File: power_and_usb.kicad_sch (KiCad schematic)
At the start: 9 parts, among them J1 USB4085-GF-A_REVB, U1 USBLC6-2SC6, U2 MCP1755T-3302E/DC

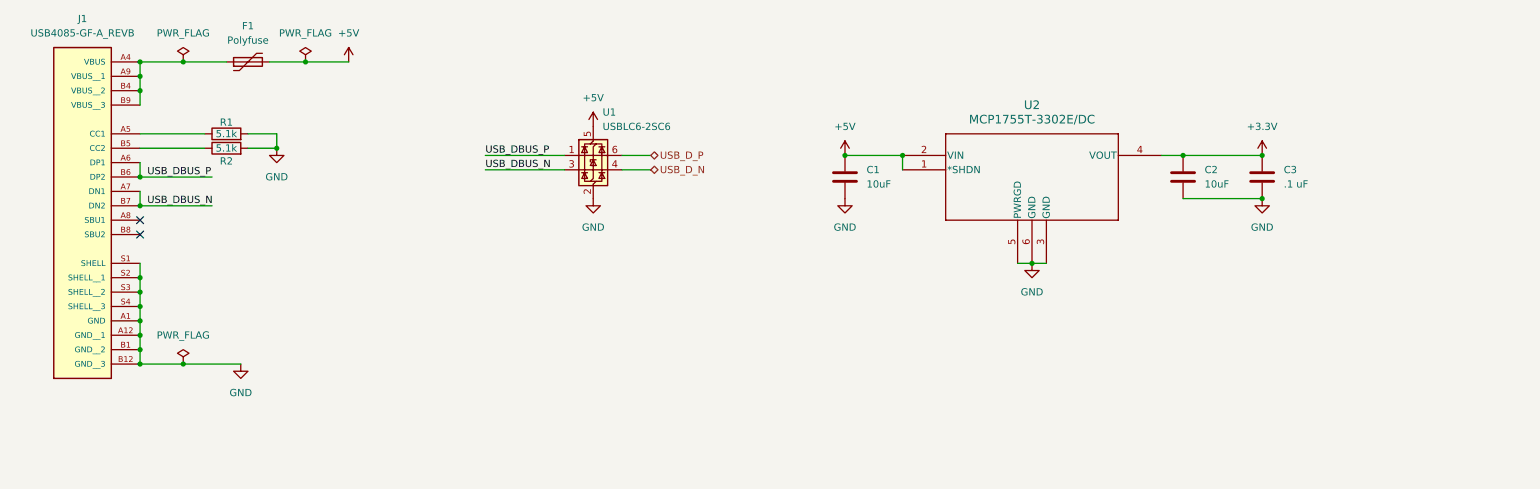
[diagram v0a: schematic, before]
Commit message: finished power, removed stm symbol from library
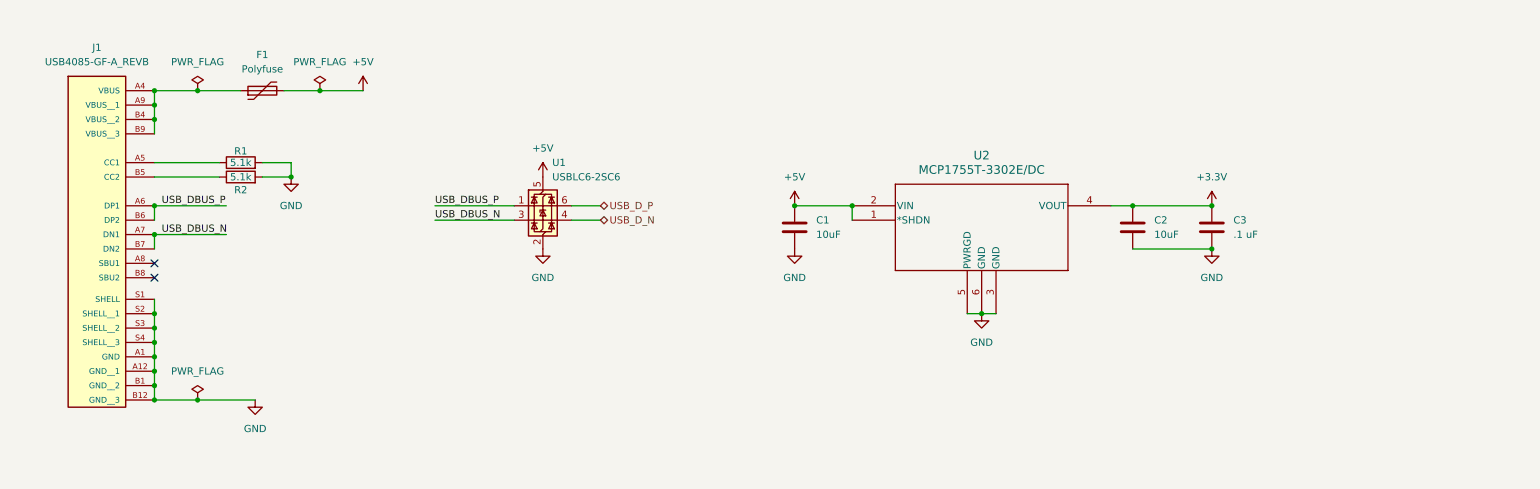
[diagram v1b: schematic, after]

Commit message: remapped stm32
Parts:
- C3: value .1 uF -> 0.1 uF
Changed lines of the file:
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@@
 		)
 		(instances
+			(project "power_and_usb"
+				(path "/b6a035cc-edeb-4159-8781-9f0e3e36ae83"
+					(reference "J1")
+					(unit 1)
+				)
+			)
 			(project "octo_keyboard"
 				(path "/e2f6b5f5-4c68-42ad-a343-f16c1cb3ab86/6d3060b6-5cde-4c96-8702-b6db72026b7d"
@@
 		)
 		(instances
+			(project "power_and_usb"
+				(path "/b6a035cc-edeb-4159-8781-9f0e3e36ae83"
+					(reference "R2")
+					(unit 1)
+				)
+			)
 			(project "octo_keyboard"
 				(path "/e2f6b5f5-4c68-42ad-a343-f16c1cb3ab86/6d3060b6-5cde-4c96-8702-b6db72026b7d"
@@
 		)
 		(instances
+			(project "power_and_usb"
+				(path "/b6a035cc-edeb-4159-8781-9f0e3e36ae83"
+					(reference "C1")
+					(unit 1)
+				)
+			)
 			(project "octo_keyboard"
 				(path "/e2f6b5f5-4c68-42ad-a343-f16c1cb3ab86/6d3060b6-5cde-4c96-8702-b6db72026b7d"
@@
 		)
 		(instances
+			(project "power_and_usb"
+				(path "/b6a035cc-edeb-4159-8781-9f0e3e36ae83"
+					(reference "#PWR03")
+					(unit 1)
+				)
+			)
 			(project "octo_keyboard"
 				(path "/e2f6b5f5-4c68-42ad-a343-f16c1cb3ab86/6d3060b6-5cde-4c96-8702-b6db72026b7d"
@@
 		)
 		(instances
+			(project "power_and_usb"
+				(path "/b6a035cc-edeb-4159-8781-9f0e3e36ae83"
+					(reference "#FLG01")
+					(unit 1)
+				)
+			)
 			(project "octo_keyboard"
 				(path "/e2f6b5f5-4c68-42ad-a343-f16c1cb3ab86/6d3060b6-5cde-4c96-8702-b6db72026b7d"
@@
 		)
 		(instances
+			(project "power_and_usb"
+				(path "/b6a035cc-edeb-4159-8781-9f0e3e36ae83"
+					(reference "#PWR05")
+					(unit 1)
+				)
+			)
 			(project "octo_keyboard"
 				(path "/e2f6b5f5-4c68-42ad-a343-f16c1cb3ab86/6d3060b6-5cde-4c96-8702-b6db72026b7d"
@@
 		)
 		(instances
+			(project "power_and_usb"
+				(path "/b6a035cc-edeb-4159-8781-9f0e3e36ae83"
+					(reference "#PWR08")
+					(unit 1)
+				)
+			)
 			(project "octo_keyboard"
 				(path "/e2f6b5f5-4c68-42ad-a343-f16c1cb3ab86/6d3060b6-5cde-4c96-8702-b6db72026b7d"
@@
 		)
 		(instances
+			(project "power_and_usb"
+				(path "/b6a035cc-edeb-4159-8781-9f0e3e36ae83"
+					(reference "#PWR01")
+					(unit 1)
+				)
+			)
 			(project "octo_keyboard"
 				(path "/e2f6b5f5-4c68-42ad-a343-f16c1cb3ab86/6d3060b6-5cde-4c96-8702-b6db72026b7d"
@@
 		)
 		(instances
+			(project "power_and_usb"
+				(path "/b6a035cc-edeb-4159-8781-9f0e3e36ae83"
+					(reference "#FLG02")
+					(unit 1)
+				)
+			)
 			(project "octo_keyboard"
 				(path "/e2f6b5f5-4c68-42ad-a343-f16c1cb3ab86/6d3060b6-5cde-4c96-8702-b6db72026b7d"
@@
 		)
 		(instances
+			(project "power_and_usb"
+				(path "/b6a035cc-edeb-4159-8781-9f0e3e36ae83"
+					(reference "C2")
+					(unit 1)
+				)
+			)
 			(project "octo_keyboard"
 				(path "/e2f6b5f5-4c68-42ad-a343-f16c1cb3ab86/6d3060b6-5cde-4c96-8702-b6db72026b7d"
@@
 		)
 		(instances
+			(project "power_and_usb"
+				(path "/b6a035cc-edeb-4159-8781-9f0e3e36ae83"
+					(reference "#PWR02")
+					(unit 1)
+				)
+			)
 			(project "octo_keyboard"
 				(path "/e2f6b5f5-4c68-42ad-a343-f16c1cb3ab86/6d3060b6-5cde-4c96-8702-b6db72026b7d"
@@
 		)
 		(instances
+			(project "power_and_usb"
+				(path "/b6a035cc-edeb-4159-8781-9f0e3e36ae83"
+					(reference "#FLG03")
+					(unit 1)
+				)
+			)
 			(project "octo_keyboard"
 				(path "/e2f6b5f5-4c68-42ad-a343-f16c1cb3ab86/6d3060b6-5cde-4c96-8702-b6db72026b7d"
@@
 		)
 		(instances
+			(project "power_and_usb"
+				(path "/b6a035cc-edeb-4159-8781-9f0e3e36ae83"
+					(reference "F1")
+					(unit 1)
+				)
+			)
 			(project "octo_keyboard"
 				(path "/e2f6b5f5-4c68-42ad-a343-f16c1cb3ab86/6d3060b6-5cde-4c96-8702-b6db72026b7d"
@@
 		)
 		(instances
+			(project "power_and_usb"
+				(path "/b6a035cc-edeb-4159-8781-9f0e3e36ae83"
+					(reference "U2")
+					(unit 1)
+				)
+			)
 			(project "octo_keyboard"
 				(path "/e2f6b5f5-4c68-42ad-a343-f16c1cb3ab86/6d3060b6-5cde-4c96-8702-b6db72026b7d"
@@
 		)
 		(instances
+			(project "power_and_usb"
+				(path "/b6a035cc-edeb-4159-8781-9f0e3e36ae83"
+					(reference "#PWR04")
+					(unit 1)
+				)
+			)
 			(project "octo_keyboard"
 				(path "/e2f6b5f5-4c68-42ad-a343-f16c1cb3ab86/6d3060b6-5cde-4c96-8702-b6db72026b7d"
@@
 		)
 		(instances
+			(project "power_and_usb"
+				(path "/b6a035cc-edeb-4159-8781-9f0e3e36ae83"
+					(reference "#PWR07")
+					(unit 1)
+				)
+			)
 			(project "octo_keyboard"
 				(path "/e2f6b5f5-4c68-42ad-a343-f16c1cb3ab86/6d3060b6-5cde-4c96-8702-b6db72026b7d"
@@
 		)
 		(instances
+			(project "power_and_usb"
+				(path "/b6a035cc-edeb-4159-8781-9f0e3e36ae83"
+					(reference "#PWR06")
+					(unit 1)
+				)
+			)
 			(project "octo_keyboard"
 				(path "/e2f6b5f5-4c68-42ad-a343-f16c1cb3ab86/6d3060b6-5cde-4c96-8702-b6db72026b7d"
@@
 		)
 		(instances
+			(project "power_and_usb"
+				(path "/b6a035cc-edeb-4159-8781-9f0e3e36ae83"
+					(reference "#PWR09")
+					(unit 1)
+				)
+			)
 			(project "octo_keyboard"
 				(path "/e2f6b5f5-4c68-42ad-a343-f16c1cb3ab86/6d3060b6-5cde-4c96-8702-b6db72026b7d"
@@
 		)
 		(instances
+			(project "power_and_usb"
+				(path "/b6a035cc-edeb-4159-8781-9f0e3e36ae83"
+					(reference "R1")
+					(unit 1)
+				)
+			)
 			(project "octo_keyboard"
 				(path "/e2f6b5f5-4c68-42ad-a343-f16c1cb3ab86/6d3060b6-5cde-4c96-8702-b6db72026b7d"
@@
 		)
 		(instances
+			(project "power_and_usb"
+				(path "/b6a035cc-edeb-4159-8781-9f0e3e36ae83"
+					(reference "#PWR010")
+					(unit 1)
+				)
+			)
 			(project "octo_keyboard"
 				(path "/e2f6b5f5-4c68-42ad-a343-f16c1cb3ab86/6d3060b6-5cde-4c96-8702-b6db72026b7d"
@@
 		)
 		(instances
+			(project "power_and_usb"
+				(path "/b6a035cc-edeb-4159-8781-9f0e3e36ae83"
+					(reference "U1")
+					(unit 1)
+				)
+			)
 			(project "octo_keyboard"
 				(path "/e2f6b5f5-4c68-42ad-a343-f16c1cb3ab86/6d3060b6-5cde-4c96-8702-b6db72026b7d"
@@
 			)
 		)
-		(property "Value" ".1 uF"
+		(property "Value" "0.1 uF"
 			(at 236.22 58.4199 0)
 			(show_name no)
@@
 		)
 		(instances
-			(project "octo_keyboard"
-				(path "/e2f6b5f5-4c68-42ad-a343-f16c1cb3ab86/6d3060b6-5cde-4c96-8702-b6db72026b7d"
+			(project "power_and_usb"
+				(path "/b6a035cc-edeb-4159-8781-9f0e3e36ae83"
 					(reference "C3")
 					(unit 1)
 				)
 			)
-		)
-	)
+			(project "octo_keyboard"
+				(path "/e2f6b5f5-4c68-42ad-a343-f16c1cb3ab86/6d3060b6-5cde-4c96-8702-b6db72026b7d"
+					(reference "C3")
+					(unit 1)
+				)
+			)
+		)
+	)
+	(sheet_instances
+		(path "/"
+			(page "1")
+		)
+	)
+	(embedded_fonts no)
 )

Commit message: power documentation
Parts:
- removed J1: USB4085-GF-A_REVB, USB4085-GF-A_REVB:GCT_USB4085-GF-A_REVB, symbol KeyboardSymbols:USB4085-GF-A_REVB
- added J1: USB_C_Receptacle_USB2.0_16P, symbol Connector:USB_C_Receptacle_USB2.0_16P
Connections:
- net GND: now also J1.A1 (GND), J1.A12 (GND), J1.B1 (GND), J1.B12 (GND), J1.SH (SHIELD)
- net USB_DBUS_N: now also J1.A7 (D-), J1.B7 (D-)
- net USB_DBUS_P: now also J1.A6 (D+), J1.B6 (D+)
- net at F1.1: now also J1.A4 (VBUS), J1.A9 (VBUS), J1.B4 (VBUS), J1.B9 (VBUS)
- net at R1.1: now also J1.A5 (CC1)
- net at R2.1: now also J1.B5 (CC2)
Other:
- note added: "Linear Voltage Regulator (LDO) 5V -> 3.3V"
- note added: "TVS Array"
- note added: "USB-C Female Receptable"
- moved on the sheet: C1, C2, C3, F1, R1, R2, U1, U2
